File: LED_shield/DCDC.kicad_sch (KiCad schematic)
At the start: 10 parts, among them U401 TPS565208

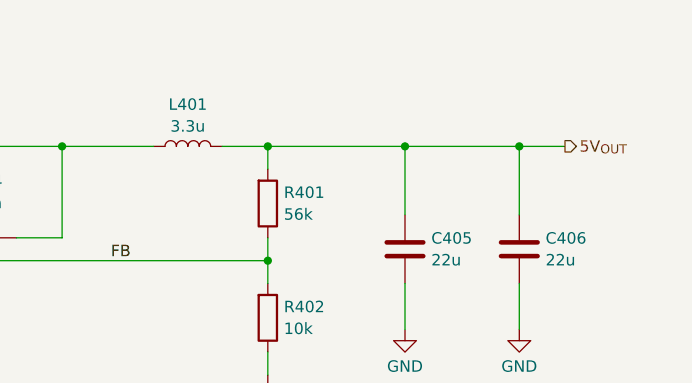
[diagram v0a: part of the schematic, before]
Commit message: Add missing LCSC partnumbers
Also fixed grouping in PCB
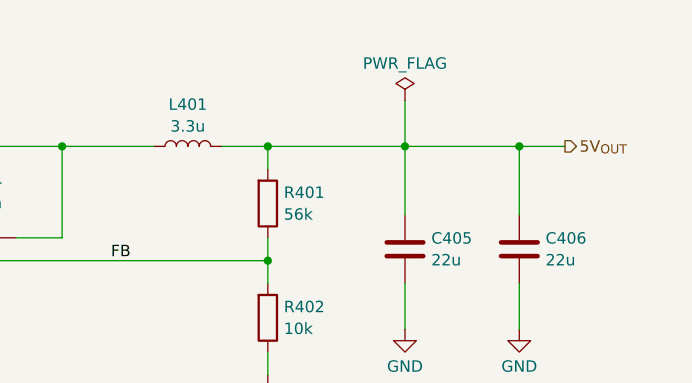
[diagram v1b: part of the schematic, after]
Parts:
- R402: LCSC (none) -> C25197
- U401: LCSC (none) -> C2650336
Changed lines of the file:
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@@
+	(wire
+		(pts
+			(xy 200.66 71.12) (xy 200.66 76.2)
+		)
+		(stroke
+			(width 0)
+			(type default)
+		)
+	)
 	(wire
 		(pts
@@
 			)
 		)
+		(property "LCSC" "C2650336"
+			(at 124.46 86.36 0)
+			(effects
+				(font
+					(size 1.27 1.27)
+				)
+				(hide yes)
+			)
+		)
 		(pin "3"
 		)
@@
 	)
 	(symbol
+		(lib_id "power:PWR_FLAG")
+		(at 200.66 71.12 0)
+		(unit 1)
+		(exclude_from_sim no)
+		(in_bom yes)
+		(on_board yes)
+		(dnp no)
+		(fields_autoplaced yes)
+		(property "Reference" "#FLG01"
+			(at 200.66 69.215 0)
+			(effects
+				(font
+					(size 1.27 1.27)
+				)
+				(hide yes)
+			)
+		)
+		(property "Value" "PWR_FLAG"
+			(at 200.66 66.9869 0)
+			(effects
+				(font
+					(size 1.27 1.27)
+				)
+			)
+		)
+		(property "Footprint" ""
+			(at 200.66 71.12 0)
+			(effects
+				(font
+					(size 1.27 1.27)
+				)
+				(hide yes)
+			)
+		)
+		(property "Datasheet" "~"
+			(at 200.66 71.12 0)
+			(effects
+				(font
+					(size 1.27 1.27)
+				)
+				(hide yes)
+			)
+		)
+		(property "Description" "Special symbol for telling ERC where power comes from"
+			(at 200.66 71.12 0)
+			(effects
+				(font
+					(size 1.27 1.27)
+				)
+				(hide yes)
+			)
+		)
+		(pin "1"
+		)
+		(instances
+			(project "LED_shield"
+				(path "/1ea5d53d-438b-4931-b69a-e3b85be65776/e840c4ed-09f9-4c51-97a0-e8f2864c789b/156257bd-e623-42b7-ac56-4691a34e7916"
+					(reference "#FLG01")
+					(unit 1)
+				)
+				(path "/1ea5d53d-438b-4931-b69a-e3b85be65776/e840c4ed-09f9-4c51-97a0-e8f2864c789b/1c08a009-198f-43f7-8708-fe9162167235"
+					(reference "#FLG03")
+					(unit 1)
+				)
+				(path "/1ea5d53d-438b-4931-b69a-e3b85be65776/e840c4ed-09f9-4c51-97a0-e8f2864c789b/b7dbf37f-d5cb-4685-b9a3-f5efa9990cf1"
+					(reference "#FLG05")
+					(unit 1)
+				)
+				(path "/1ea5d53d-438b-4931-b69a-e3b85be65776/e840c4ed-09f9-4c51-97a0-e8f2864c789b/b8d97433-cca3-43bc-98c6-1973c495da29"
+					(reference "#FLG06")
+					(unit 1)
+				)
+				(path "/1ea5d53d-438b-4931-b69a-e3b85be65776/e840c4ed-09f9-4c51-97a0-e8f2864c789b/c5d13b95-b629-467f-87f8-0b3f3a9ebb72"
+					(reference "#FLG04")
+					(unit 1)
+				)
+				(path "/1ea5d53d-438b-4931-b69a-e3b85be65776/e840c4ed-09f9-4c51-97a0-e8f2864c789b/d7448860-4103-48e8-9f80-95ab28f05e94"
+					(reference "#FLG02")
+					(unit 1)
+				)
+			)
+		)
+	)
+	(symbol
 		(lib_id "Device:C")
 		(at 200.66 87.63 0)
@@
 			)
 		)
-		(property "LCSC" ""
+		(property "LCSC" "C25197"
 			(at 185.42 95.25 0)
 			(effects
